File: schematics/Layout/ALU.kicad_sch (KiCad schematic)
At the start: 11 parts

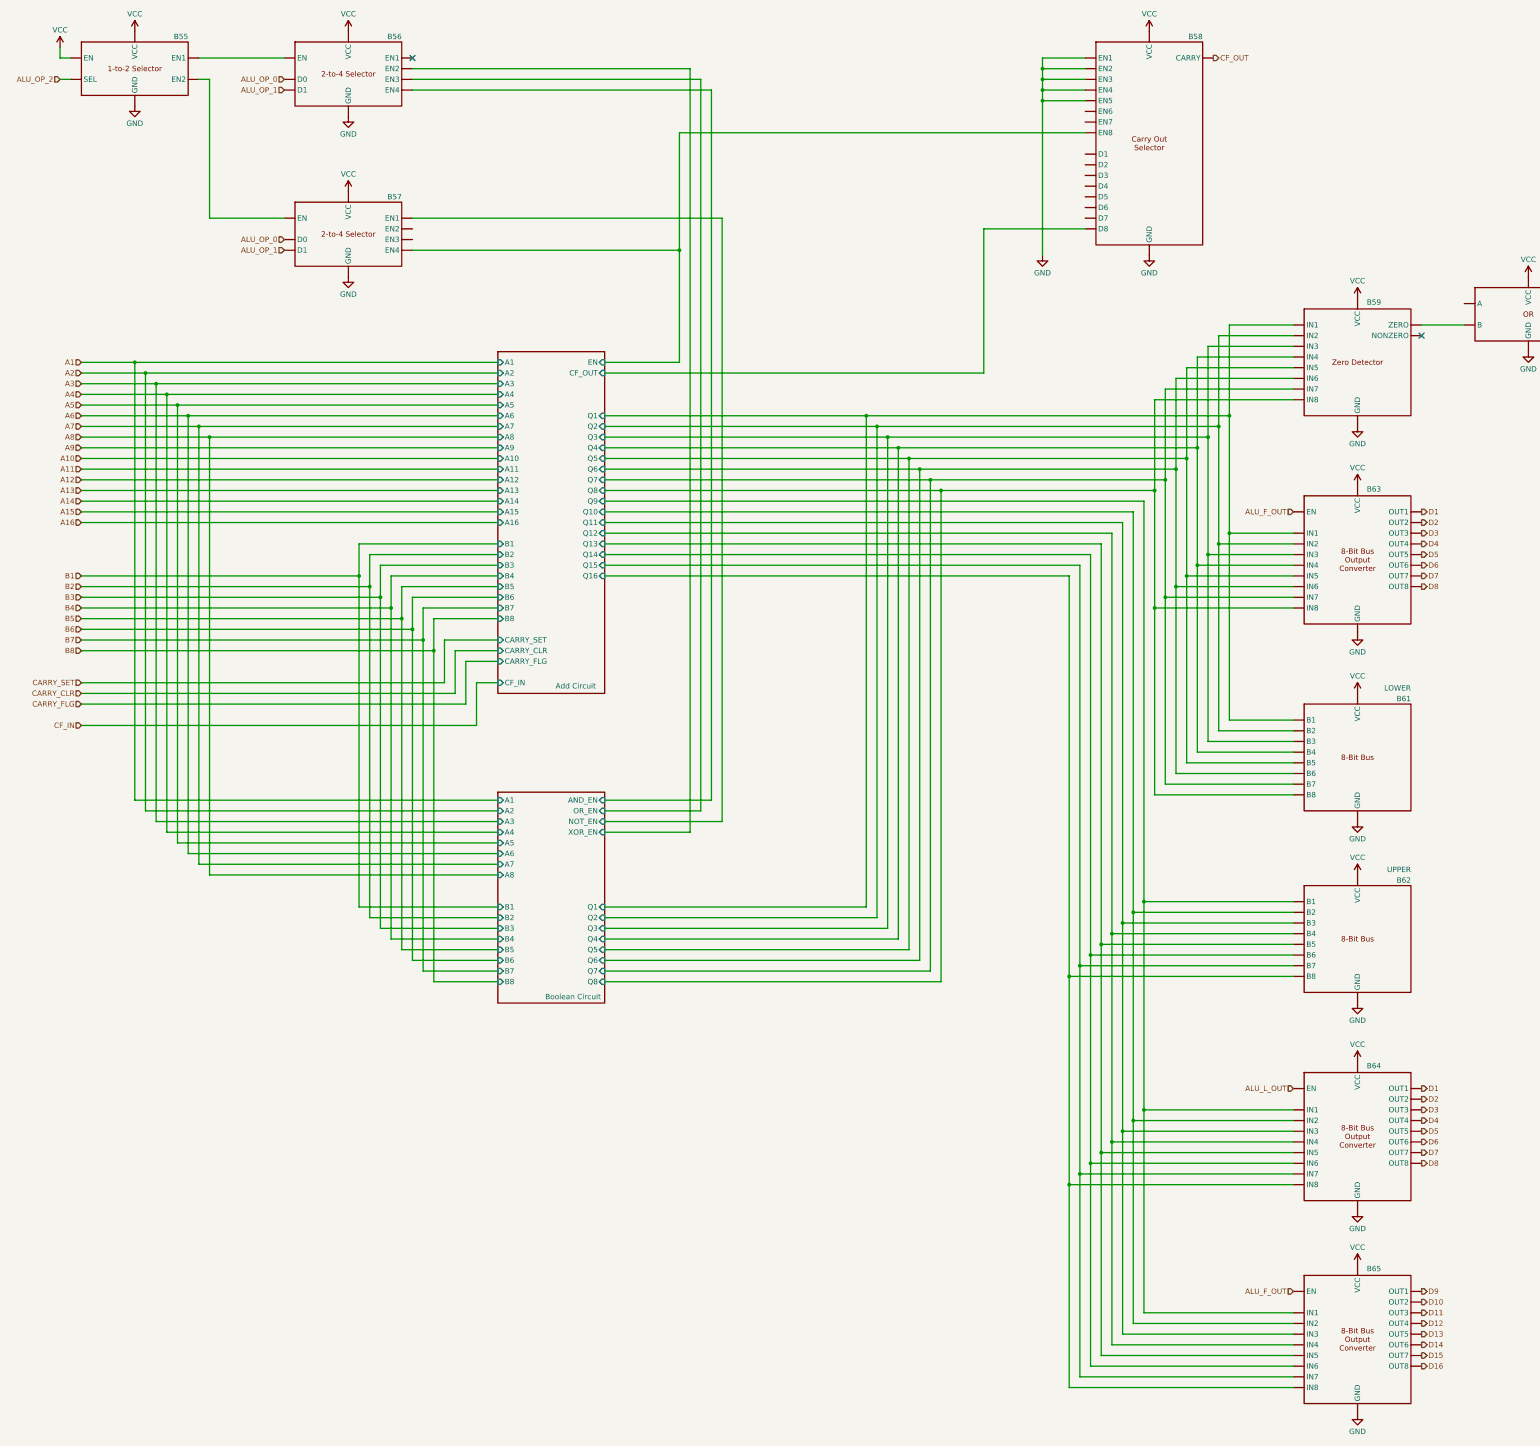
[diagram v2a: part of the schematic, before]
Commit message: Update with new Shift symbol, diagram the rest of the ALU and more instruction decoder boards.
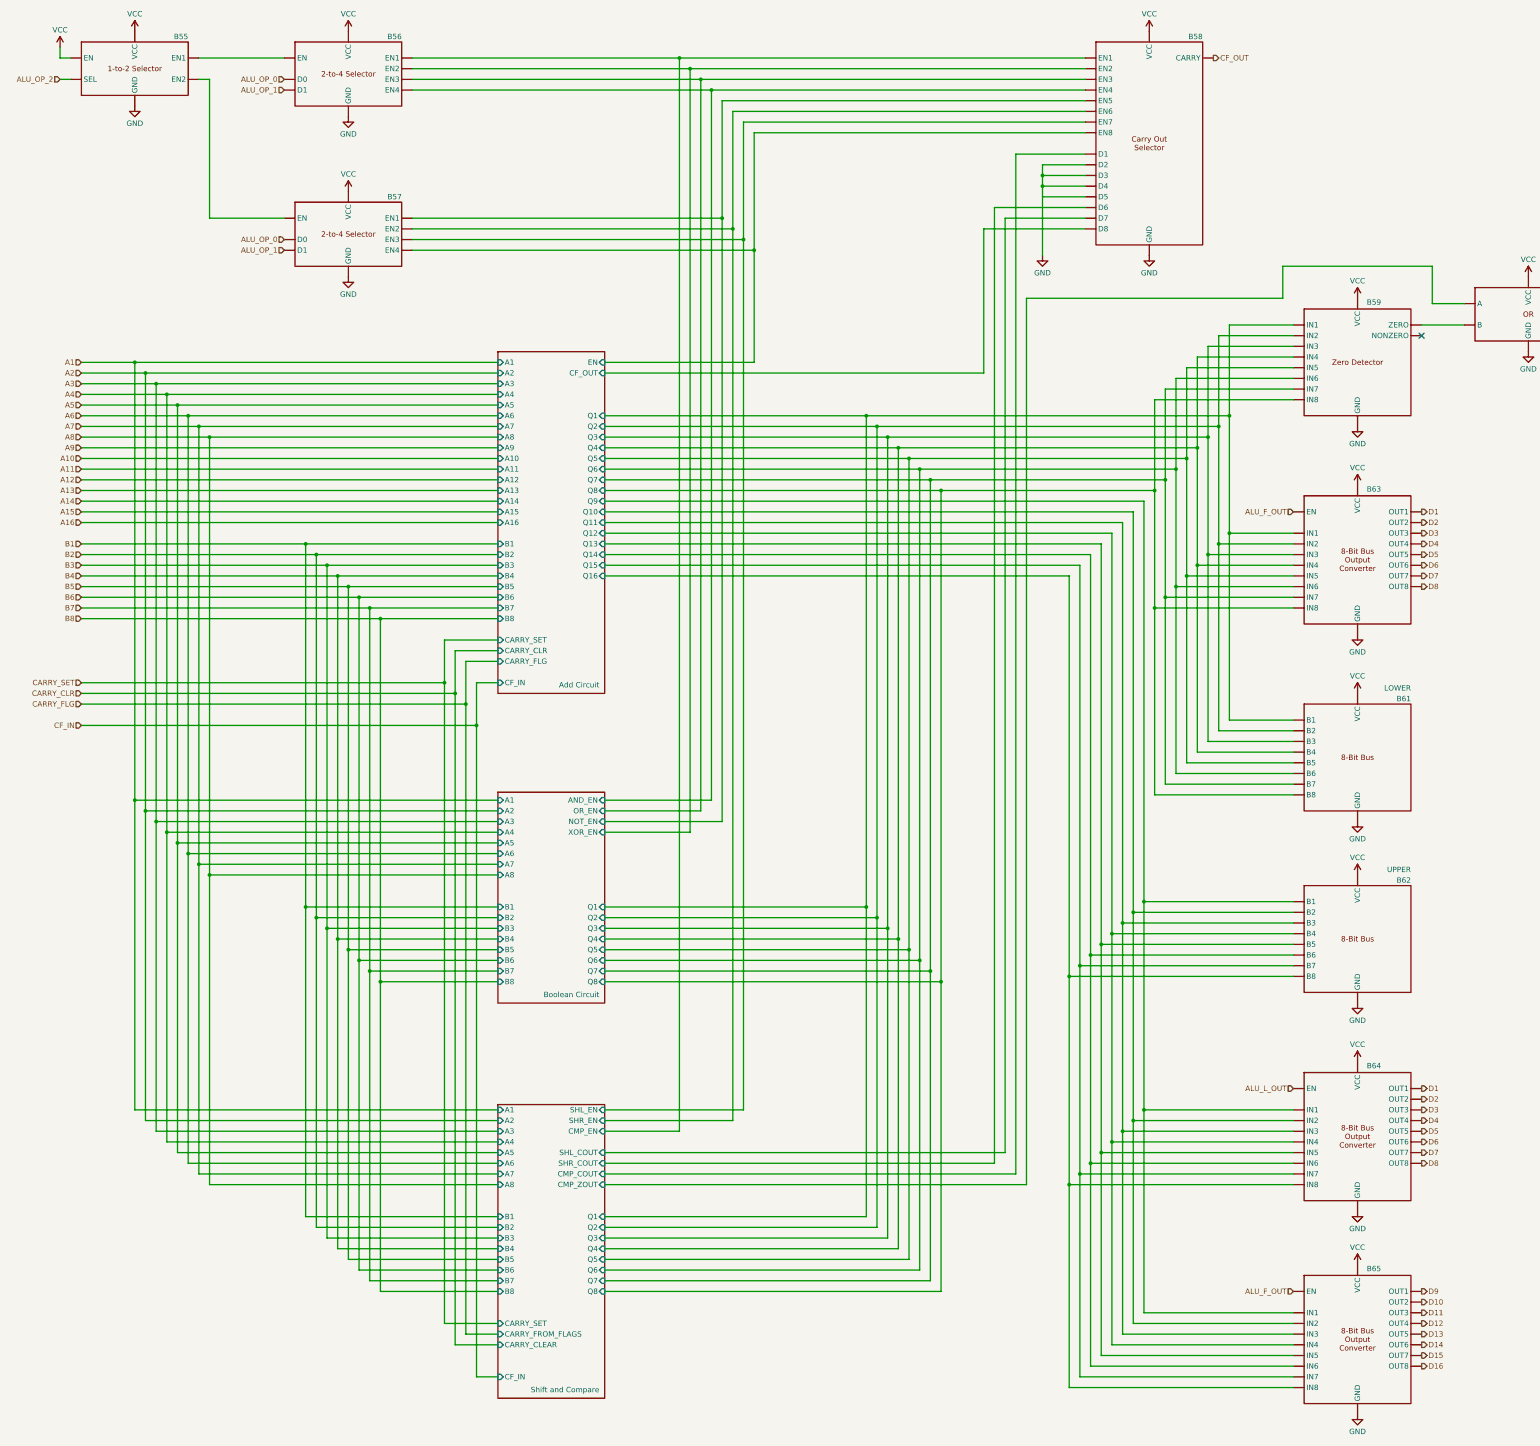
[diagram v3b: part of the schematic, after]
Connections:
- net Boolean Circuit/AND_EN: now also B58. (CARRY)
- net Boolean Circuit/NOT_EN: now also B58. (CARRY)
- net Boolean Circuit/OR_EN: now also B58. (CARRY)
- net Boolean Circuit/XOR_EN: now also B58. (CARRY)
- new net: B55. (EN2), B57. (EN4)
- new net: B55. (EN2), B56. (EN4)
- new net: B59. (NONZERO), B60. (OUT)
- new net Shift and Compare/CMP_COUT: B58. (CARRY)
- new net Shift and Compare/CMP_EN: B56. (EN4), B58. (CARRY)
- new net Shift and Compare/CMP_ZOUT: B60. (OUT)
- new net Shift and Compare/SHL_COUT: B58. (CARRY)
- new net Shift and Compare/SHL_EN: B57. (EN4), B58. (CARRY)
- new net Shift and Compare/SHR_COUT: B58. (CARRY)
- new net Shift and Compare/SHR_EN: B57. (EN4), B58. (CARRY)
- no-connect marks 2 -> 1
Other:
- added sheet Shift and Compare (Shift and Compare.kicad_sch)
